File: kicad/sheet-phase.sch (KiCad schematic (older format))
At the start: 10 parts, among them U8 IFX007T

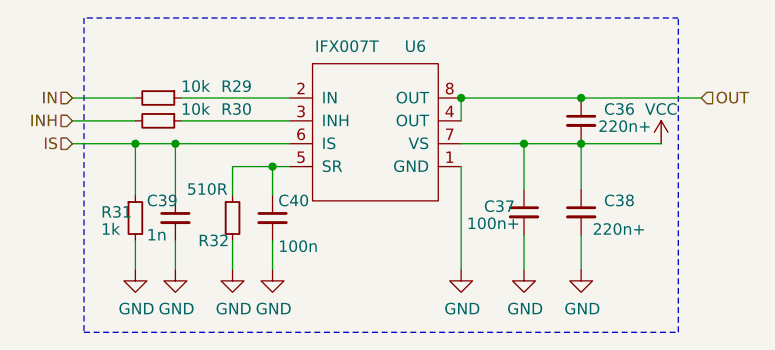
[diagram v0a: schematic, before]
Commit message: adding solder bridge and more vias under driver
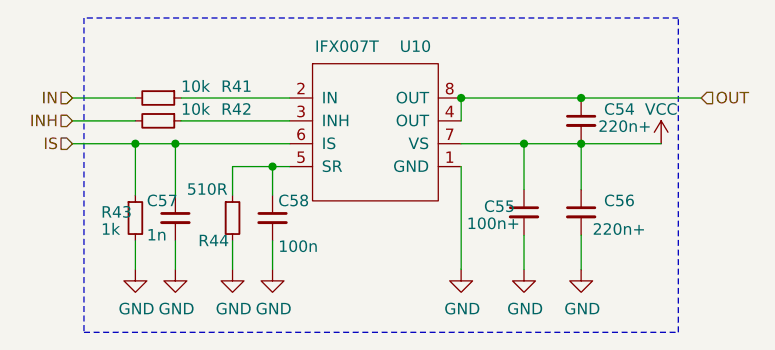
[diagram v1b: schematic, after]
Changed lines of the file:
@@
 $Descr A4 11693 8268
 encoding utf-8
-Sheet 7 12
+Sheet 5 12
 Title ""
 Date ""
@@
 AR Path="/5FEA8158/5FFEA8C3/5FF5DEB1" Ref="#PWR0105"  Part="1"
 AR Path="/6003038D/5FFEA8C3/5FF5DEB1" Ref="#PWR073"  Part="1"
-F 0 "#PWR073" H 4150 3125 50  0001 C CNN
+F 0 "#PWR0105" H 4150 3125 50  0001 C CNN
 F 1 "GND" H 4155 3202 50  0000 C CNN
 F 2 "" H 4150 3375 50  0001 C CNN
@@
 AR Path="/5FEA8158/5FFEA8C3/5FF5E7D2" Ref="#PWR0104"  Part="1"
 AR Path="/6003038D/5FFEA8C3/5FF5E7D2" Ref="#PWR072"  Part="1"
-F 0 "#PWR072" H 3325 3125 50  0001 C CNN
+F 0 "#PWR0104" H 3325 3125 50  0001 C CNN
 F 1 "GND" H 3330 3202 50  0000 C CNN
 F 2 "" H 3325 3375 50  0001 C CNN
@@
 AR Path="/5FEA8158/5FFEA8C3/5FF5F36A" Ref="R44"  Part="1"
 AR Path="/6003038D/5FFEA8C3/5FF5F36A" Ref="R32"  Part="1"
-F 0 "R32" H 3000 3050 50  0000 L CNN
+F 0 "R44" H 3000 3050 50  0000 L CNN
 F 1 "510R" H 2950 3275 50  0000 L CNN
 F 2 "Resistor_SMD:R_0402_1005Metric" H 3150 3150 50  0001 C CNN
@@
 AR Path="/5FEA8158/5FFEA8C3/5FF60820" Ref="#PWR0106"  Part="1"
 AR Path="/6003038D/5FFEA8C3/5FF60820" Ref="#PWR074"  Part="1"
-F 0 "#PWR074" H 4425 3125 50  0001 C CNN
+F 0 "#PWR0106" H 4425 3125 50  0001 C CNN
 F 1 "GND" H 4430 3202 50  0000 C CNN
 F 2 "" H 4425 3375 50  0001 C CNN
@@
 AR Path="/5FEA8158/5FFEA8C3/5FF63F9D" Ref="C58"  Part="1"
 AR Path="/6003038D/5FFEA8C3/5FF63F9D" Ref="C40"  Part="1"
-F 0 "C40" H 3350 3225 50  0000 L CNN
+F 0 "C58" H 3350 3225 50  0000 L CNN
 F 1 "100n" H 3350 3025 50  0000 L CNN
 F 2 "Capacitor_SMD:C_0402_1005Metric" H 3325 3150 50  0001 C CNN
@@
 AR Path="/5FEA8158/5FFEA8C3/5FF65732" Ref="R42"  Part="1"
 AR Path="/6003038D/5FFEA8C3/5FF65732" Ref="R30"  Part="1"
-F 0 "R30" V 2775 3000 50  0000 L CNN
+F 0 "R42" V 2775 3000 50  0000 L CNN
 F 1 "10k" V 2775 2825 50  0000 L CNN
 F 2 "Resistor_SMD:R_0402_1005Metric" H 2825 2725 50  0001 C CNN
@@
 AR Path="/5FEA8158/5FFEA8C3/5FF67BB2" Ref="R41"  Part="1"
 AR Path="/6003038D/5FFEA8C3/5FF67BB2" Ref="R29"  Part="1"
-F 0 "R29" V 2775 2900 50  0000 L CNN
+F 0 "R41" V 2775 2900 50  0000 L CNN
 F 1 "10k" V 2775 2725 50  0000 L CNN
 F 2 "Resistor_SMD:R_0402_1005Metric" H 2825 2625 50  0001 C CNN
@@
 AR Path="/5FEA8158/5FFEA8C3/5FF6D8E7" Ref="#PWR0103"  Part="1"
 AR Path="/6003038D/5FFEA8C3/5FF6D8E7" Ref="#PWR071"  Part="1"
-F 0 "#PWR071" H 3150 3125 50  0001 C CNN
+F 0 "#PWR0103" H 3150 3125 50  0001 C CNN
 F 1 "GND" H 3155 3202 50  0000 C CNN
 F 2 "" H 3150 3375 50  0001 C CNN
@@
 AR Path="/5FEA8158/5FFEA8C3/5FF6E097" Ref="R43"  Part="1"
 AR Path="/6003038D/5FFEA8C3/5FF6E097" Ref="R31"  Part="1"
-F 0 "R31" H 2575 3175 50  0000 L CNN
+F 0 "R43" H 2575 3175 50  0000 L CNN
 F 1 "1k" H 2575 3100 50  0000 L CNN
 F 2 "Resistor_SMD:R_0402_1005Metric" H 2725 3150 50  0001 C CNN
@@
 AR Path="/5FEA8158/5FFEA8C3/5FF6E488" Ref="C57"  Part="1"
 AR Path="/6003038D/5FFEA8C3/5FF6E488" Ref="C39"  Part="1"
-F 0 "C39" H 2775 3225 50  0000 L CNN
+F 0 "C57" H 2775 3225 50  0000 L CNN
 F 1 "1n" H 2775 3075 50  0000 L CNN
 F 2 "Capacitor_SMD:C_0402_1005Metric" H 2900 3150 50  0001 C CNN
@@
 AR Path="/5FEA8158/5FFEA8C3/5FF6E8C7" Ref="#PWR0101"  Part="1"
 AR Path="/6003038D/5FFEA8C3/5FF6E8C7" Ref="#PWR069"  Part="1"
-F 0 "#PWR069" H 2725 3125 50  0001 C CNN
+F 0 "#PWR0101" H 2725 3125 50  0001 C CNN
 F 1 "GND" H 2730 3202 50  0000 C CNN
 F 2 "" H 2725 3375 50  0001 C CNN
@@
 AR Path="/5FEA8158/5FFEA8C3/5FF6EC7A" Ref="#PWR0102"  Part="1"
 AR Path="/6003038D/5FFEA8C3/5FF6EC7A" Ref="#PWR070"  Part="1"
-F 0 "#PWR070" H 2900 3125 50  0001 C CNN
+F 0 "#PWR0102" H 2900 3125 50  0001 C CNN
 F 1 "GND" H 2905 3202 50  0000 C CNN
 F 2 "" H 2900 3375 50  0001 C CNN
@@
 AR Path="/5FEA8158/5FFEA8C3/5FF7826D" Ref="C54"  Part="1"
 AR Path="/6003038D/5FFEA8C3/5FF7826D" Ref="C36"  Part="1"
-F 0 "C36" H 4775 2775 50  0000 L CNN
+F 0 "C54" H 4775 2775 50  0000 L CNN
 F 1 "220n+" H 4750 2700 50  0000 L CNN
 F 2 "Capacitor_SMD:C_0603_1608Metric" H 4675 2725 50  0001 C CNN
@@
 AR Path="/5FEA8158/5FFEA8C3/5FF7DB12" Ref="#PWR0107"  Part="1"
 AR Path="/6003038D/5FFEA8C3/5FF7DB12" Ref="#PWR075"  Part="1"
-F 0 "#PWR075" H 4675 3125 50  0001 C CNN
+F 0 "#PWR0107" H 4675 3125 50  0001 C CNN
 F 1 "GND" H 4680 3202 50  0000 C CNN
 F 2 "" H 4675 3375 50  0001 C CNN
@@
 AR Path="/5FEA8158/5FFEA8C3/5FF60692" Ref="C55"  Part="1"
 AR Path="/6003038D/5FFEA8C3/5FF60692" Ref="C37"  Part="1"
-F 0 "C37" H 4250 3150 50  0000 L CNN
+F 0 "C55" H 4250 3150 50  0000 L CNN
 F 1 "100n+" H 4175 3075 50  0000 L CNN
 F 2 "Capacitor_SMD:C_0603_1608Metric" H 4425 3125 50  0001 C CNN
@@
 AR Path="/5FEA8158/5FFEA8C3/5FF5CF24" Ref="U10"  Part="1"
 AR Path="/6003038D/5FFEA8C3/5FF5CF24" Ref="U6"  Part="1"
-F 0 "U6" H 3950 2550 50  0000 C CNN
+F 0 "U10" H 3950 2550 50  0000 C CNN
 F 1 "IFX007T" H 3650 2550 50  0000 C CNN
 F 2 "Package_TO_SOT_SMD:TO-263-7_TabPin8" H 3500 2475 50  0001 C CNN
@@
 AR Path="/5FEA8158/5FFEA82A/5FFC809F" Ref="#PWR092"  Part="1"
 AR Path="/5FEA8158/5FFEA8C3/5FFC809F" Ref="#PWR0100"  Part="1"
-F 0 "#PWR068" H 5025 2675 50  0001 C CNN
+F 0 "#PWR0100" H 5025 2675 50  0001 C CNN
 F 1 "VCC" H 5025 2975 50  0000 C CNN
 F 2 "" H 5025 2825 50  0001 C CNN
@@
 AR Path="/5FEA8158/5FFEA8C3/5FFFAD84" Ref="C56"  Part="1"
 AR Path="/6003038D/5FFEA8C3/5FFFAD84" Ref="C38"  Part="1"
-F 0 "C38" H 4775 3175 50  0000 L CNN
+F 0 "C56" H 4775 3175 50  0000 L CNN
 F 1 "220n+" H 4725 3050 50  0000 L CNN
 F 2 "Capacitor_SMD:C_0603_1608Metric" H 4675 3125 50  0001 C CNN
